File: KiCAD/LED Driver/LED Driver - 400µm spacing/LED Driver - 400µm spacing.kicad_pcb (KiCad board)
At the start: 2 copper layers, 16.5 x 9 mm, 16 parts, among them Q1 Q_NMOS_GSD, U1 LP5868TRKPR, U2 ATtiny3226, U3 XC61GC3002HR-G

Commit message: Working draft of programmer/charger board
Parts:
- added BT1: LiPo Cell, Custom:LPM0940, B.Cu at (54.7, 34.2)
- TP2: footprint Custom:1mm pad -> Custom:1mm pad x4
- moved Q1 0.63 mm to (51.0, 37.1)
- moved C2 0.57 mm to (53.0, 37.8)
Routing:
- net Net-(Q1-G): track 1.31 -> 2.05 mm
- net GND: track 41.5 -> 41.2 mm, vias 21 -> 20

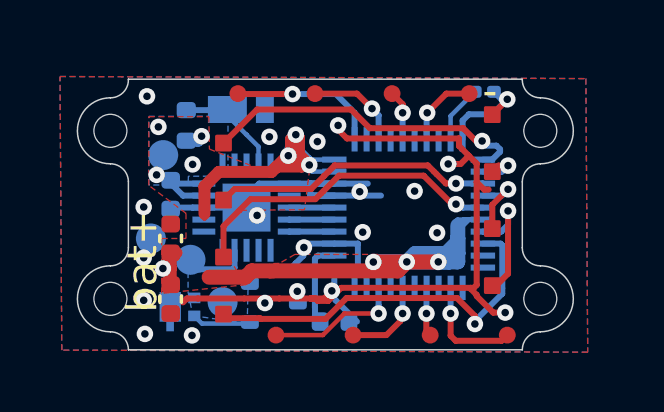
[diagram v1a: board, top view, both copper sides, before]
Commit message: Remove status pads for charger as DC-DC converter is required
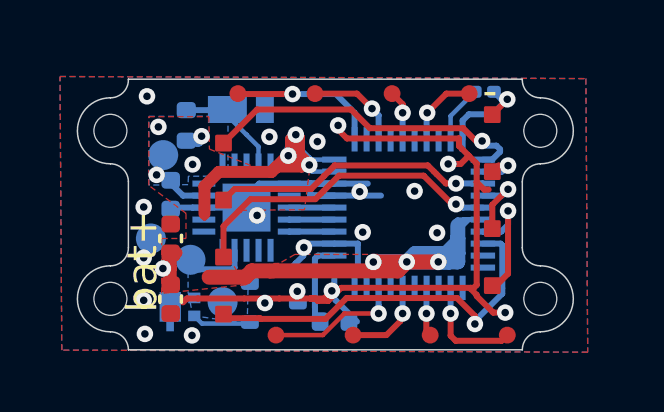
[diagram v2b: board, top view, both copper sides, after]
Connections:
- U2 pad 5: +BATT -> unconnected-(U2-0~/PA4-Pad5)
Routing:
- net +BATT: track 40.6 -> 39.5 mm
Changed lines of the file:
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@@
 	(net 49 "Net-(D2-K)")
 	(net 50 "unconnected-(U2-3{slash}PA7-Pad8)")
+	(net 51 "unconnected-(U2-0~{slash}PA4-Pad5)")
 	(footprint "Capacitor_SMD:C_0402_1005Metric"
 		(layer "F.Cu")
@@
 			(size 0.2032 0.762)
 			(layers "B.Cu" "B.Paste" "B.Mask")
-			(net 48 "+BATT")
+			(net 51 "unconnected-(U2-0~{slash}PA4-Pad5)")
 			(pinfunction "0~/PA4")
-			(pintype "input")
+			(pintype "input+no_connect")
 		)
 		(pad "6" smd rect
@@
 	)
 	(segment
-		(start 48.6152 33.159998)
-		(end 47.519998 33.159998)
-		(width 0.2)
-		(layer "B.Cu")
-		(net 48)
-	)
-	(segment
 		(start 54.269998 35.77)
 		(end 55.38 35.77)
@@
 		(polygon
 			(pts
-				(xy 49.68 36.26) (xy 49.64 36.27) (xy 49.43 36.27) (xy 49.43 36.47) (xy 49.43 36.47) (xy 49.84 36.71)
-				(xy 50.11 36.71) (xy 50.12 36.26)
+				(xy 49.68 36.26) (xy 49.64 36.27) (xy 49.43 36.27) (xy 49.43 36.47) (xy 49.84 36.71) (xy 50.11 36.71)
+				(xy 50.12 36.26)
+			)
+		)
+	)
+	(zone
+		(net 0)
+		(net_name "")
+		(layer "B.Mask")
+		(hatch edge 0.5)
+		(connect_pads
+			(clearance 0.15)
+		)
+		(min_thickness 0.1)
+		(filled_areas_thickness no)
+		(fill yes
+			(thermal_gap 0.5)
+			(thermal_bridge_width 0.5)
+		)
+		(polygon
+			(pts
+				(xy 52.96 34.26) (xy 52.96 34.46) (xy 51.43 34.46) (xy 51.43 34.26)
+			)
+		)
+	)
+	(zone
+		(net 0)
+		(net_name "")
+		(layer "B.Mask")
+		(hatch edge 0.5)
+		(connect_pads
+			(clearance 0.15)
+		)
+		(min_thickness 0.1)
+		(filled_areas_thickness no)
+		(fill yes
+			(thermal_gap 0.5)
+			(thermal_bridge_width 0.5)
+		)
+		(polygon
+			(pts
+				(xy 52.96 33.86) (xy 52.96 34.06) (xy 51.43 34.06) (xy 51.43 33.86)
 			)
 		)

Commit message: Move bolts 1 mm
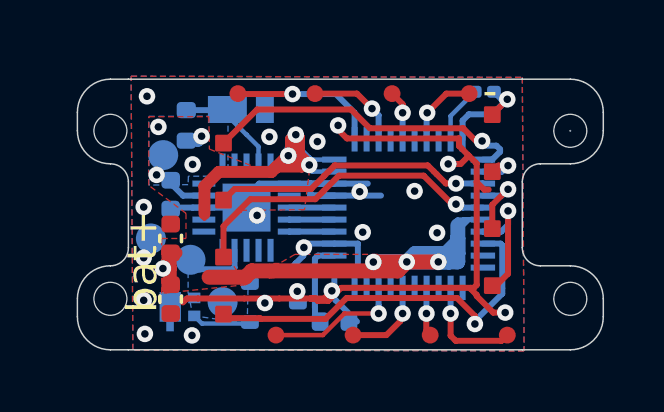
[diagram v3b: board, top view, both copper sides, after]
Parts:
- moved H1 1.00 mm to (60.8, 31.4)
- moved H2 1.00 mm to (60.8, 37.0)
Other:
- board size 16.5 x 9 mm -> 17.5 x 9 mm
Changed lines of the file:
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@@
 			(layer "F.Fab")
 		)
+		(fp_text user "${REFERENCE}"
+			(at 0 0 90)
+			(layer "F.Fab")
+			(effects
+				(font
+					(size 0.25 0.25)
+					(thickness 0.04)
+				)
+			)
+		)
 		(pad "1" smd roundrect
 			(at -0.48 0 90)
@@
 			(layer "F.Fab")
 		)
+		(fp_text user "${REFERENCE}"
+			(at 0 0 90)
+			(layer "F.Fab")
+			(effects
+				(font
+					(size 0.25 0.25)
+					(thickness 0.04)
+				)
+			)
+		)
 		(pad "1" smd roundrect
 			(at -0.48 0 90)
@@
 			)
 		)
-		(fp_text user "${REFERENCE}"
-			(at 0 0 180)
-			(unlocked yes)
+		(fp_text user "*"
+			(at -1.0414 1 180)
 			(layer "B.Fab")
 			(effects
@@
 		)
 		(fp_text user "*"
-			(at -1.0414 1 180)
+			(at -1.0414 1 0)
 			(layer "B.Fab")
 			(effects
@@
 			)
 		)
-		(fp_text user "*"
-			(at -1.0414 1 0)
+		(fp_text user "${REFERENCE}"
+			(at 0 0 180)
+			(unlocked yes)
 			(layer "B.Fab")
 			(effects
@@
 	(footprint "Custom:M1 hole"
 		(layer "B.Cu")
-		(at 59.83 37 180)
+		(at 60.83 37 180)
 		(property "Reference" "H2"
 			(at -0.15 1.42 0)
@@
 	(footprint "Custom:M1 hole"
 		(layer "B.Cu")
-		(at 59.83 31.4 180)
+		(at 60.83 31.4 180)
 		(property "Reference" "H1"
 			(at -0.15 1.42 0)
@@
 		(net 25)
 	)
+	(gr_circle
+		(center 45.5 31.4)
+		(end 45.560827 31.4)
+		(stroke
+			(width 0.01)
+			(type default)
+		)
+		(fill none)
+		(layer "B.Cu")
+	)
 	(gr_rect
 		(start 49.04 33.48)
@@
 	)
 	(gr_arc
+		(start 45.5 32.5)
+		(mid 44.722183 32.177817)
+		(end 44.4 31.4)
+		(stroke
+			(width 0.05)
+			(type default)
+		)
+		(layer "Edge.Cuts")
+	)
+	(gr_line
+		(start 44.4 37.6)
+		(end 44.4 37)
+		(stroke
+			(width 0.05)
+			(type default)
+		)
+		(layer "Edge.Cuts")
+	)
+	(gr_arc
 		(start 46.1 35.3)
 		(mid 45.924264 35.724264)
@@
 		(layer "Edge.Cuts")
 	)
+	(gr_line
+		(start 46.1 29.68)
+		(end 45.5 29.68)
+		(stroke
+			(width 0.05)
+			(type default)
+		)
+		(layer "Edge.Cuts")
+	)
 	(gr_arc
 		(start 59.23 33.1)
@@
 		(layer "Edge.Cuts")
 	)
+	(gr_line
+		(start 60.83 32.5)
+		(end 59.83 32.5)
+		(stroke
+			(width 0.05)
+			(type default)
+		)
+		(layer "Edge.Cuts")
+	)
 	(gr_arc
 		(start 59.83 35.9)
-		(mid 60.93 37)
-		(end 59.83 38.1)
+		(mid 59.405736 35.724264)
+		(end 59.23 35.3)
 		(stroke
 			(width 0.05)
@@
 		(layer "Edge.Cuts")
 	)
-	(gr_arc
-		(start 45.5 38.1)
-		(mid 44.4 37)
-		(end 45.5 35.9)
+	(gr_line
+		(start 61.93 30.78)
+		(end 61.93 31.4)
 		(stroke
 			(width 0.05)
@@
 		(layer "Edge.Cuts")
 	)
-	(gr_arc
-		(start 59.83 35.9)
-		(mid 59.405736 35.724264)
-		(end 59.23 35.3)
+	(gr_line
+		(start 60.83 35.9)
+		(end 59.83 35.9)
+		(stroke
+			(width 0.05)
+			(type default)
+		)
+		(layer "Edge.Cuts")
+	)
+	(gr_line
+		(start 44.4 31.4)
+		(end 44.4 30.78)
 		(stroke
 			(width 0.05)
@@
 	)
 	(gr_arc
-		(start 45.5 32.5)
-		(mid 44.4 31.4)
-		(end 45.5 30.3)
+		(start 61.93 31.4)
+		(mid 61.607817 32.177817)
+		(end 60.83 32.5)
+		(stroke
+			(width 0.05)
+			(type default)
+		)
+		(layer "Edge.Cuts")
+	)
+	(gr_line
+		(start 46.1 38.7)
+		(end 45.5 38.7)
 		(stroke
 			(width 0.05)
@@
 	(gr_line
 		(start 59.23 29.68)
-		(end 59.23 29.7)
+		(end 60.83 29.68)
 		(stroke
 			(width 0.05)
@@
 		(layer "Edge.Cuts")
 	)
-	(gr_arc
-		(start 59.83 30.3)
-		(mid 59.405736 30.124264)
-		(end 59.23 29.7)
+	(gr_line
+		(start 61.93 37)
+		(end 61.93 37.6)
 		(stroke
 			(width 0.05)
@@
 	)
 	(gr_arc
-		(start 46.1 29.7)
-		(mid 45.924264 30.124264)
-		(end 45.5 30.3)
+		(start 44.4 30.78)
+		(mid 44.722183 30.002183)
+		(end 45.5 29.68)
 		(stroke
 			(width 0.05)
@@
 	)
 	(gr_arc
-		(start 59.83 30.3)
-		(mid 60.93 31.4)
-		(end 59.83 32.5)
+		(start 60.83 29.68)
+		(mid 61.607817 30.002183)
+		(end 61.93 30.78)
 		(stroke
 			(width 0.05)
@@
 		(layer "Edge.Cuts")
 	)
-	(gr_line
-		(start 46.1 33.1)
-		(end 46.1 35.3)
+	(gr_circle
+		(center 60.83 31.4)
+		(end 60.84 31.4)
 		(stroke
-			(width 0.05)
+			(width 0.01)
 			(type default)
 		)
+		(fill none)
 		(layer "Edge.Cuts")
 	)
 	(gr_arc
-		(start 45.5 38.1)
-		(mid 45.924264 38.275736)
-		(end 46.1 38.7)
+		(start 45.5 38.7)
+		(mid 44.722183 38.377817)
+		(end 44.4 37.6)
 		(stroke
 			(width 0.05)
@@
 	)
 	(gr_line
-		(start 46.1 29.68)
-		(end 46.1 29.7)
+		(start 46.1 33.1)
+		(end 46.1 35.3)
 		(stroke
 			(width 0.05)
@@
 		(layer "Edge.Cuts")
 	)
-	(gr_line
-		(start 59.23 29.68)
-		(end 46.1 29.68)
+	(gr_arc
+		(start 60.83 35.9)
+		(mid 61.607817 36.222183)
+		(end 61.93 37)
 		(stroke
 			(width 0.05)
@@
 	)
 	(gr_arc
-		(start 59.23 38.7)
-		(mid 59.405736 38.275736)
-		(end 59.83 38.1)
+		(start 61.93 37.6)
+		(mid 61.607817 38.377817)
+		(end 60.83 38.7)
+		(stroke
+			(width 0.05)
+			(type default)
+		)
+		(layer "Edge.Cuts")
+	)
+	(gr_line
+		(start 59.23 29.68)
+		(end 46.1 29.68)
 		(stroke
 			(width 0.05)
@@
 		(layer "Edge.Cuts")
 	)
+	(gr_arc
+		(start 44.4 37)
+		(mid 44.722183 36.222183)
+		(end 45.5 35.9)
+		(stroke
+			(width 0.05)
+			(type default)
+		)
+		(layer "Edge.Cuts")
+	)
+	(gr_line
+		(start 59.23 38.7)
+		(end 60.83 38.7)
+		(stroke
+			(width 0.05)
+			(type default)
+		)
+		(layer "Edge.Cuts")
+	)
 	(gr_rect
 		(start 48.73 29.7)
@@
 	)
 	(gr_circle
+		(center 45.5 37)
+		(end 45.51 37)
+		(stroke
+			(width 0.01)
+			(type default)
+		)
+		(fill none)
+		(layer "User.1")
+	)
+	(gr_circle
 		(center 47.26 32.21)
 		(end 47.76 32.21)
@@
 		(polygon
 			(pts
-				(xy 43.82 29.59) (xy 61.35 29.66) (xy 61.41 38.78) (xy 43.88 38.71)
+				(xy 46.19 29.58) (xy 59.23 29.62) (xy 59.29 38.74) (xy 46.25 38.7)
 			)
 		)
